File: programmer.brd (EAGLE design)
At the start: 41.1 x 23 mm, 20 parts, among them IC1 74ABT125DB, U1 ATMEGA8U2, X1 16MHz

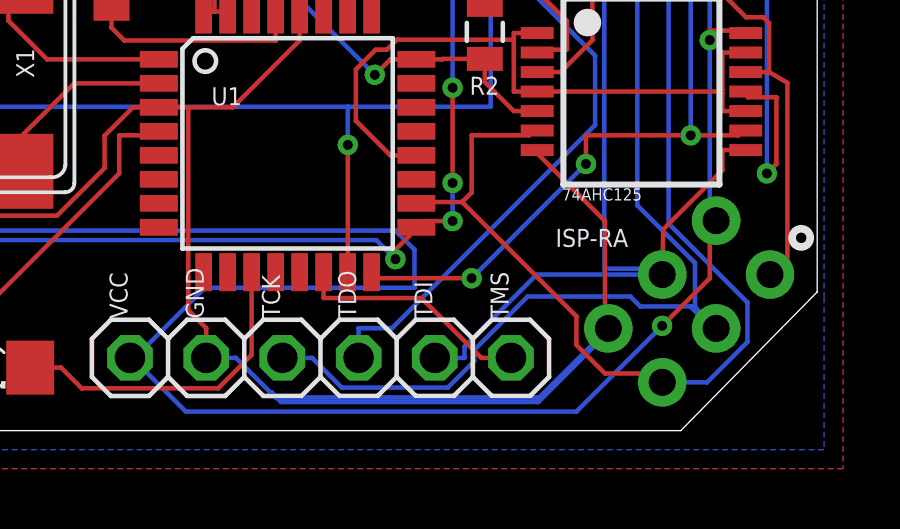
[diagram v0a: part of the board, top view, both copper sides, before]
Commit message: Fixed: PB0 replaced with RST for JTAG header.
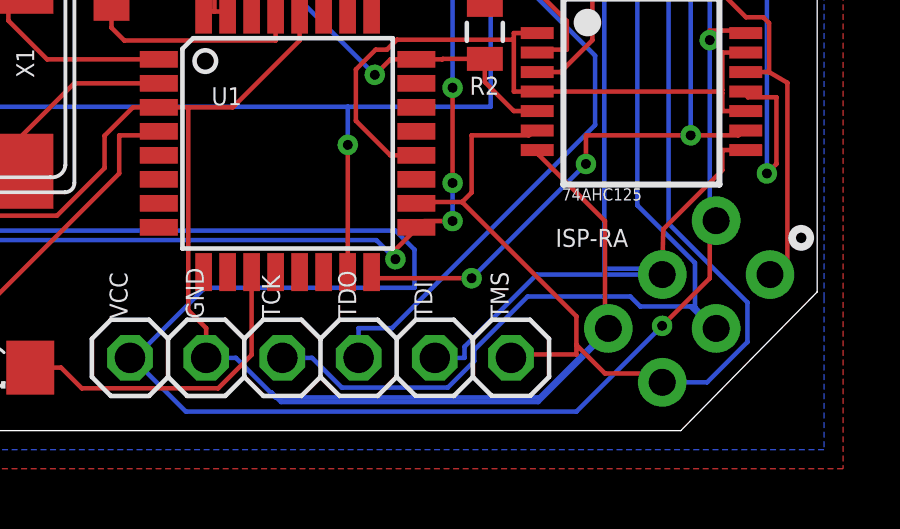
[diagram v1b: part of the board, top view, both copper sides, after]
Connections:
- removed net PB0: JP2.6, U1.14
- net RST: now also JP2.6
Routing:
- net PB0: track 7.94 -> 0.00 mm
- net RST: track 35.4 -> 37.9 mm
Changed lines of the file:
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@@
 <wire x1="35.8775" y1="1.905" x2="33.9725" y2="1.905" width="0.1524" layer="1"/>
 <wire x1="35.8775" y1="1.905" x2="35.881475" y2="1.610521875" width="0.1524" layer="1"/>
+<contactref element="JP2" pad="6"/>
+<wire x1="33.02" y1="2.54" x2="31.115" y2="2.54" width="0.1524" layer="1"/>
+<wire x1="33.02" y1="2.8575" x2="33.02" y2="2.54" width="0.1524" layer="1"/>
+<wire x1="31.115" y1="2.54" x2="30.8395" y2="2.4257" width="0.1524" layer="1"/>
 </signal>
 <signal name="MISO">
@@
 <wire x1="37.8371" y1="11.3026" x2="31.7133" y2="11.3026" width="0.1524" layer="1"/>
 </signal>
-<signal name="PB0">
-<contactref element="JP2" pad="6"/>
-<contactref element="U1" pad="14"/>
-<wire x1="30.8395" y1="2.4257" x2="29.8488" y2="2.4257" width="0.1524" layer="1"/>
-<wire x1="24.5934" y1="5.2832" x2="24.5934" y2="4.4195" width="0.1524" layer="1"/>
-<wire x1="24.5934" y1="4.4195" x2="27.855" y2="4.4195" width="0.1524" layer="1"/>
-<wire x1="27.855" y1="4.4195" x2="29.8488" y2="2.4257" width="0.1524" layer="1"/>
-</signal>
 <signal name="N$1">

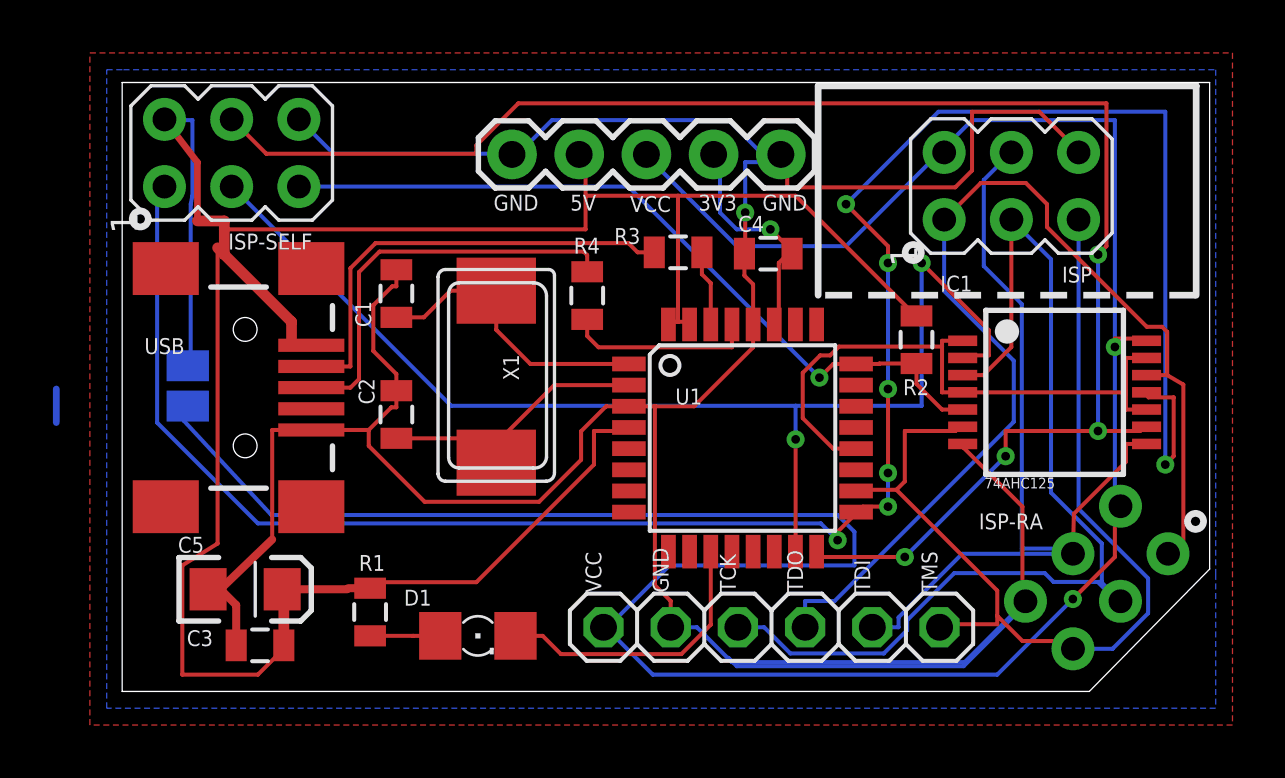
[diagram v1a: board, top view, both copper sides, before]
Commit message: Fixed miswired RESET/RST/RST-UC.
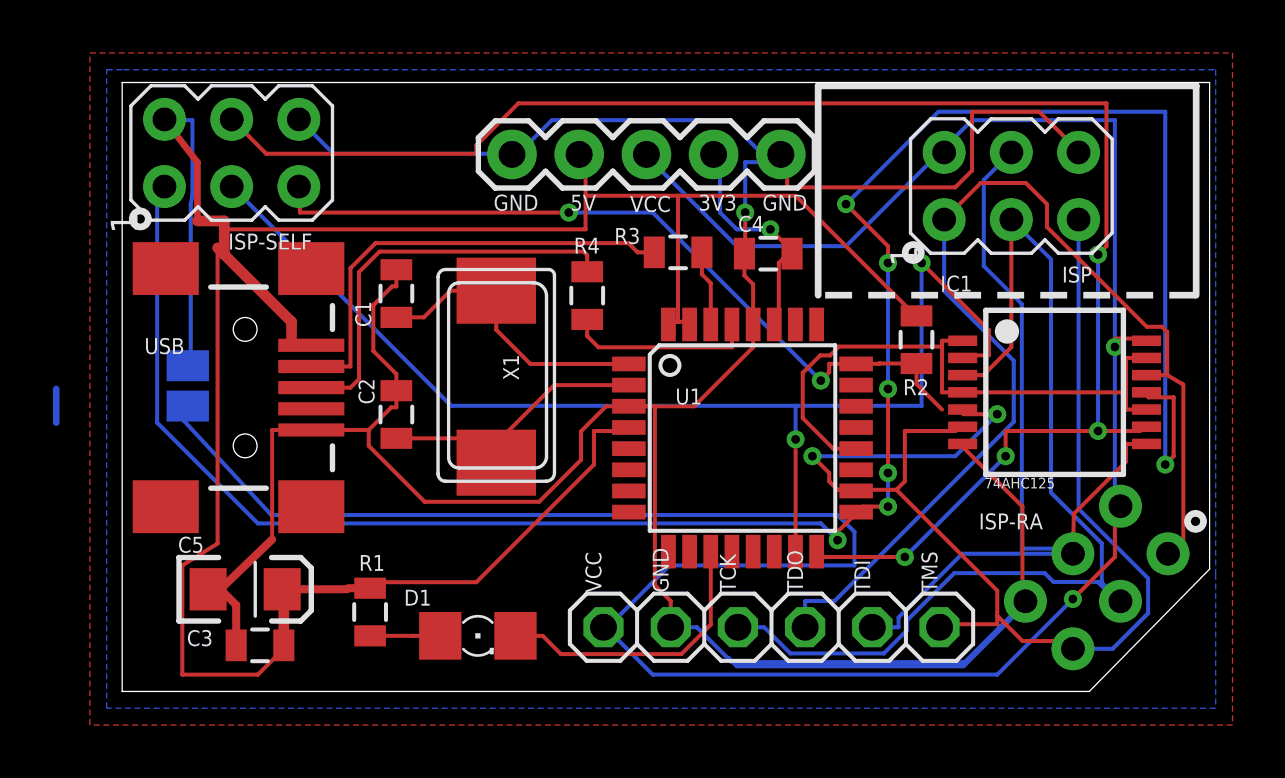
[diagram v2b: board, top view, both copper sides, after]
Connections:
- net LED renamed ACTIVITY
- new net RESET: ISP-SELF.5, R2.2, U1.24
- net RST: no longer U1.18
- net RST-UC: now also U1.18; no longer ISP-SELF.5, R2.2, U1.24
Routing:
- net RESET: track 0.00 -> 29.6 mm, vias 0 -> 2
- net RST-UC: track 29.5 -> 11.5 mm, vias 1 -> 2
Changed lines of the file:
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@@
 <contactref element="ISP" pad="5"/>
 <contactref element="ISP-RA" pad="5"/>
-<contactref element="U1" pad="18"/>
 <contactref element="IC1" pad="6"/>
 <wire x1="35.8815" y1="1.6105" x2="37.3772" y2="1.6105" width="0.1524" layer="16"/>
@@
 <wire x1="27.94" y1="7.62" x2="29.21" y2="7.62" width="0.1524" layer="1"/>
 <wire x1="31.4325" y1="9.8425" x2="31.7133" y2="10.0026" width="0.1524" layer="1"/>
-<wire x1="27.94" y1="7.62" x2="27.686" y2="7.5758" width="0.1524" layer="1"/>
 <wire x1="33.02" y1="3.81" x2="29.21" y2="7.62" width="0.1524" layer="1"/>
 <wire x1="33.02" y1="2.8575" x2="33.02" y2="3.81" width="0.1524" layer="1"/>
@@
 </signal>
 <signal name="RST-UC">
-<contactref element="U1" pad="24"/>
-<contactref element="R2" pad="2"/>
-<contactref element="ISP-SELF" pad="5"/>
+<contactref element="U1" pad="18"/>
 <contactref element="IC1" pad="5"/>
-<wire x1="26.8223" y1="12.3758" x2="26.3062" y2="11.8597" width="0.1524" layer="1"/>
-<wire x1="26.3062" y1="11.8597" x2="26.2997" y2="11.8597" width="0.1524" layer="1"/>
-<wire x1="6.6287" y1="19.0791" x2="19.0803" y2="19.0791" width="0.1524" layer="16"/>
-<wire x1="19.0803" y1="19.0791" x2="26.2997" y2="11.8597" width="0.1524" layer="16"/>
-<wire x1="27.686" y1="12.3758" x2="26.8223" y2="12.3758" width="0.1524" layer="1"/>
-<wire x1="29.9681" y1="12.392" x2="29.9681" y2="11.6191" width="0.1524" layer="1"/>
-<wire x1="29.9681" y1="11.6191" x2="30.9346" y2="10.6526" width="0.1524" layer="1"/>
-<wire x1="28.5497" y1="12.3758" x2="28.5659" y2="12.392" width="0.1524" layer="1"/>
-<wire x1="28.5659" y1="12.392" x2="29.9681" y2="12.392" width="0.1524" layer="1"/>
-<via x="26.2997" y="11.8597" extent="1-16" drill="0.3302" diameter="0.6858"/>
-<wire x1="31.7133" y1="10.6526" x2="30.9346" y2="10.6526" width="0.1524" layer="1"/>
-<wire x1="27.686" y1="12.3758" x2="28.5497" y2="12.3758" width="0.1524" layer="1"/>
-</signal>
-<signal name="LED">
+<wire x1="33.02" y1="10.4775" x2="31.75" y2="10.4775" width="0.1524" layer="1"/>
+<wire x1="31.4325" y1="8.89" x2="33.02" y2="10.4775" width="0.1524" layer="16"/>
+<wire x1="26.035" y1="8.89" x2="31.4325" y2="8.89" width="0.1524" layer="16"/>
+<wire x1="26.67" y1="8.255" x2="26.035" y2="8.89" width="0.1524" layer="1"/>
+<wire x1="26.67" y1="7.9375" x2="26.67" y2="8.255" width="0.1524" layer="1"/>
+<wire x1="26.9875" y1="7.62" x2="26.67" y2="7.9375" width="0.1524" layer="1"/>
+<wire x1="27.6225" y1="7.62" x2="26.9875" y2="7.62" width="0.1524" layer="1"/>
+<wire x1="31.75" y1="10.4775" x2="31.7133" y2="10.6526" width="0.1524" layer="1"/>
+<wire x1="27.6225" y1="7.62" x2="27.686" y2="7.5758" width="0.1524" layer="1"/>
+<via x="33.02" y="10.4775" extent="1-16" drill="0.3302"/>
+<via x="26.035" y="8.89" extent="1-16" drill="0.3302"/>
+</signal>
+<signal name="ACTIVITY">
 <contactref element="D1" pad="C"/>
 <contactref element="U1" pad="11"/>
@@
 <wire x1="-2.54" y1="11.43" x2="-2.54" y2="10.16" width="0.254" layer="16"/>
 </signal>
+<signal name="RESET">
+<contactref element="R2" pad="2"/>
+<wire x1="29.9681" y1="12.392" x2="29.9681" y2="11.6191" width="0.1524" layer="1"/>
+<wire x1="29.9681" y1="11.6191" x2="30.9346" y2="10.6526" width="0.1524" layer="1"/>
+<wire x1="28.5497" y1="12.3758" x2="28.5659" y2="12.392" width="0.1524" layer="1"/>
+<wire x1="28.5659" y1="12.392" x2="28.575" y2="12.392" width="0.1524" layer="1"/>
+<contactref element="ISP-SELF" pad="5"/>
+<contactref element="U1" pad="24"/>
+<wire x1="28.575" y1="12.392" x2="29.9681" y2="12.392" width="0.1524" layer="1"/>
+<wire x1="28.575" y1="12.3825" x2="27.94" y2="12.3825" width="0.1524" layer="1"/>
+<wire x1="27.94" y1="12.3825" x2="27.686" y2="12.3758" width="0.1524" layer="1"/>
+<wire x1="28.575" y1="12.3825" x2="28.575" y2="12.392" width="0.1524" layer="1"/>
+<wire x1="26.67" y1="12.3825" x2="27.6225" y2="12.3825" width="0.1524" layer="1"/>
+<wire x1="26.67" y1="12.065" x2="26.67" y2="12.3825" width="0.1524" layer="1"/>
+<wire x1="26.3525" y1="11.7475" x2="26.67" y2="12.065" width="0.1524" layer="1"/>
+<wire x1="20.0025" y1="18.0975" x2="26.3525" y2="11.7475" width="0.1524" layer="16"/>
+<wire x1="16.8275" y1="18.0975" x2="20.0025" y2="18.0975" width="0.1524" layer="16"/>
+<wire x1="6.6675" y1="18.0975" x2="16.8275" y2="18.0975" width="0.1524" layer="1"/>
+<wire x1="6.6675" y1="19.05" x2="6.6675" y2="18.0975" width="0.1524" layer="1"/>
+<wire x1="27.6225" y1="12.3825" x2="27.686" y2="12.3758" width="0.1524" layer="1"/>
+<wire x1="6.6675" y1="19.05" x2="6.6287" y2="19.0791" width="0.1524" layer="1"/>
+<via x="26.3525" y="11.7475" extent="1-16" drill="0.3302"/>
+<via x="16.8275" y="18.0975" extent="1-16" drill="0.3302"/>
+</signal>
 </signals>

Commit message: v1.0.1, 1 via
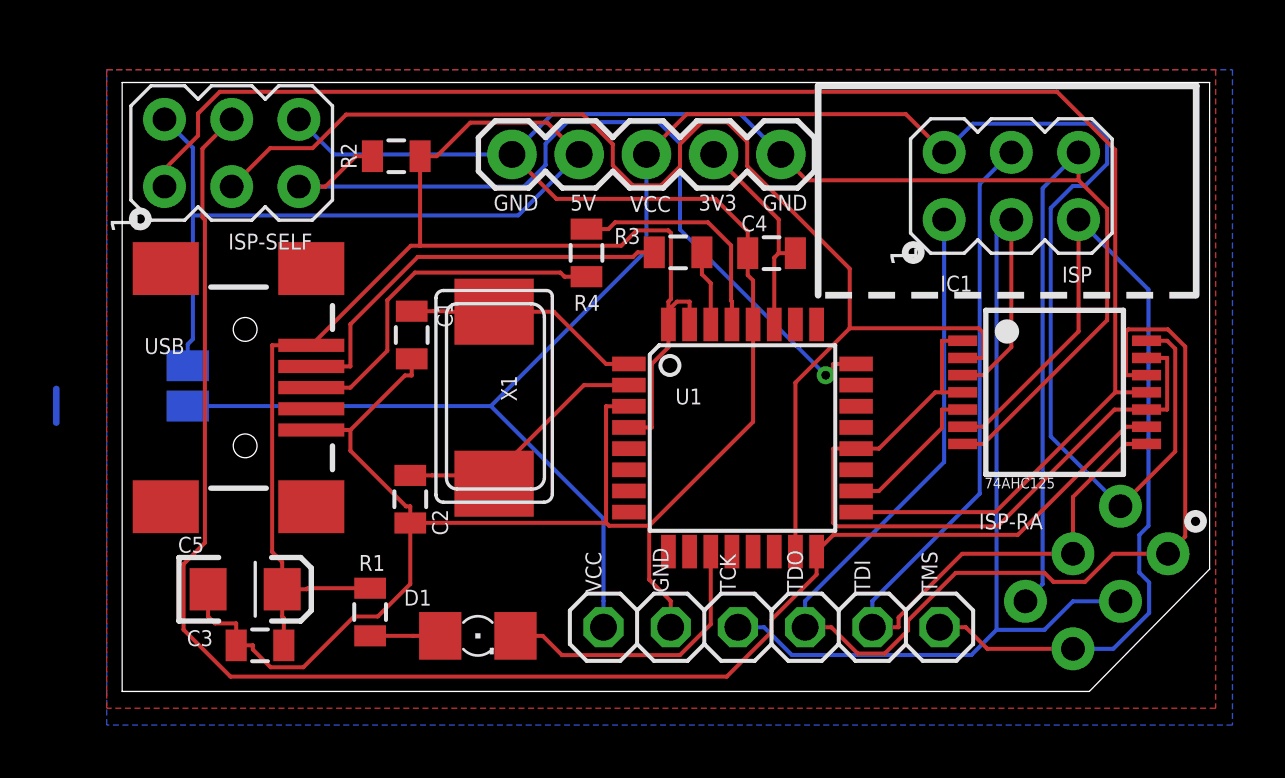
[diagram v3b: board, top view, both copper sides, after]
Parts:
- moved R2 20.8 mm to (10.3, 20.2), turned to 180 degrees
- moved C2 3.24 mm to (10.8, 7.26), turned to 270 degrees
- moved C1 1.67 mm to (10.9, 13.5), turned to 270 degrees
- moved R4 1.61 mm to (17.5, 16.6), turned to 90 degrees
- moved X1 0.80 mm to (14.0, 11.2)
- moved C4 0.13 mm to (24.5, 16.6)
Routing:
- net VCC: track 101.1 -> 77.0 mm, vias 2 -> 0
- net 5V: track 99.0 -> 78.0 mm
- net MISO-UC: track 82.1 -> 61.2 mm, vias 7 -> 0
- net RST-UC: track 11.5 -> 5.71 mm, vias 2 -> 0
- net BUFFER-OE: track 23.1 -> 28.5 mm
- net MISO: track 42.4 -> 46.8 mm
- net SCK-UC: track 46.0 -> 48.8 mm, vias 2 -> 0
- net RST: track 37.7 -> 35.2 mm
- net RESET: track 29.6 -> 31.9 mm, vias 2 -> 1
- net D+RAW: track 15.6 -> 13.4 mm
- net XTAL1: track 11.2 -> 9.04 mm
- net D+: track 7.14 -> 8.93 mm
- net GND: track 126.9 -> 128.6 mm, vias 1 -> 0
- net MOSI: track 33.2 -> 34.8 mm
- net SCK: track 40.1 -> 38.6 mm
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- added copper zone on layer 16, net VCC
- removed copper zone on layer 16, net GND
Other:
- board text added: "v1.0.1"
- board text removed: "v1.0.0"

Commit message: v1.0s.  s for squished
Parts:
- moved C3 13.7 mm to (8.20, 15.1)
- moved C5 11.1 mm to (3.29, 14.8), turned to 180 degrees
- moved ISP-RA 6.21 mm to (30.6, 4.03)
- moved JP2 6.00 mm to (18.5, 1.83)
- moved IC1 5.27 mm to (29.9, 11.4)
- moved USB 4.76 mm to (4.69, 6.72)
- moved U1 3.24 mm to (20.2, 9.06)
- moved R3 3.12 mm to (18.1, 15.4)
- moved C4 2.97 mm to (21.7, 15.4)
- moved C1 2.96 mm to (9.84, 10.7)
- moved ISP 2.68 mm to (30.9, 19.2)
- moved JP1 2.56 mm to (12.4, 19.2)
- moved D1 2.29 mm to (13.2, 4.38)
- moved R4 1.91 mm to (15.6, 16.2)
- moved R2 1.71 mm to (9.56, 18.7), turned to 270 degrees
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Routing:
- net 5V: track 78.0 -> 64.1 mm
- net MOSI: track 34.8 -> 48.4 mm
- net VCC: track 77.0 -> 67.8 mm
- net GND: track 128.6 -> 121.7 mm
- net SCK-UC: track 48.8 -> 42.9 mm
- net ACTIVITY: track 10.9 -> 5.29 mm
- net MISO-UC: track 61.2 -> 56.4 mm
- net RESET: track 31.9 -> 28.6 mm
- net MOSI-UC: track 61.9 -> 58.7 mm
- net BUFFER-OE: track 28.5 -> 25.6 mm
- net MISO: track 46.8 -> 49.4 mm
- net XTAL2: track 10.00 -> 8.12 mm
- net D+RAW: track 13.4 -> 15.2 mm
- net D+: track 8.93 -> 7.25 mm
- net XTAL1: track 9.04 -> 7.75 mm
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- added copper zone on layer 1, net 5V
- added copper zone on layer 16, net GND
- removed copper zone on layer 16, net VCC
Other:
- board size 41.1 x 23 mm -> 35.3 x 22.1 mm

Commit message: Moved ISP6 dot. Removed floating jumper connector.
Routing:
- net N$1: track 1.27 -> 0.00 mm
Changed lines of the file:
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@@
 <text x="14.9352" y="21.3106" size="0.6" layer="21" font="vector" ratio="18" rot="R180" align="bottom-center">5V</text>
 <circle x="0.635" y="17.8562" radius="0.127" width="0.6096" layer="21"/>
-<circle x="29.845" y="16.5862" radius="0.127" width="0.6096" layer="21"/>
+<circle x="26.9494" y="17.9832" radius="0.127" width="0.6096" layer="21"/>
 </plain>
 <attributes>
@@
 <wire x1="24.1319" y1="8.659" x2="23.6238" y2="8.659" width="0.1524" layer="1"/>
 </signal>
-<signal name="N$1">
-<wire x1="-2.54" y1="11.43" x2="-2.54" y2="10.16" width="0.254" layer="16"/>
-</signal>
 <signal name="RESET">
